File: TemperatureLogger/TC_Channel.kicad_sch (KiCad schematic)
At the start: 21 parts, among them J1 TC_BLOCK, U1 MAX31855KASA, U16 MCP1700x-330xxTT, U4 ISO7741DBQR

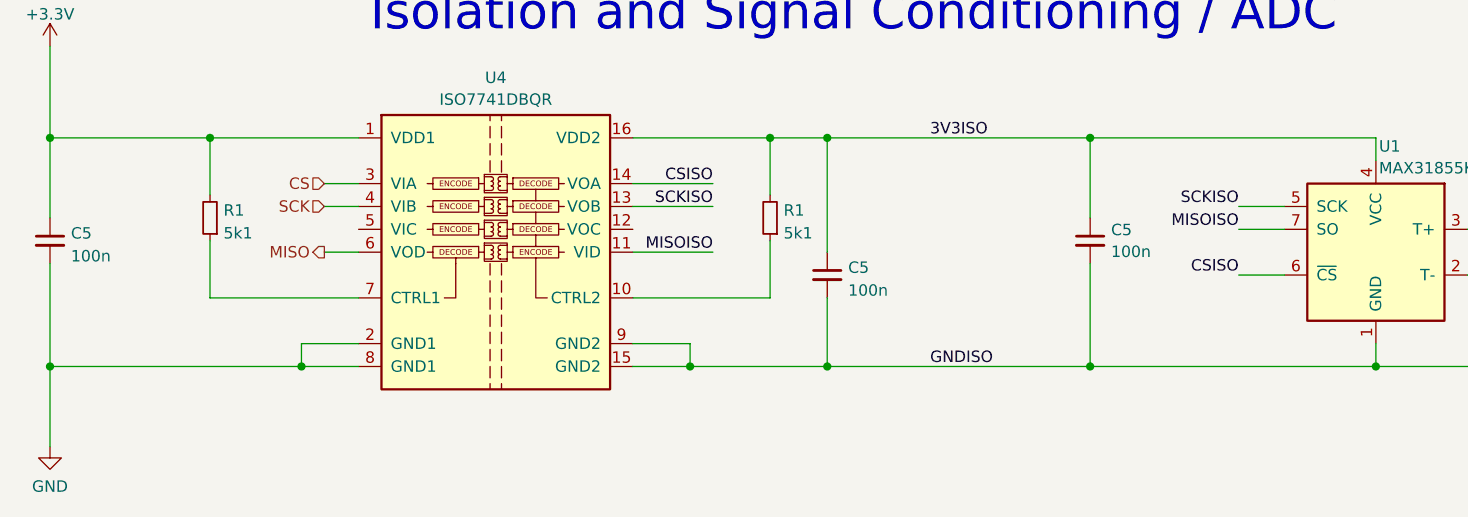
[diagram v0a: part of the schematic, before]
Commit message: added external flash and corrected issue with output disable for digital isolators
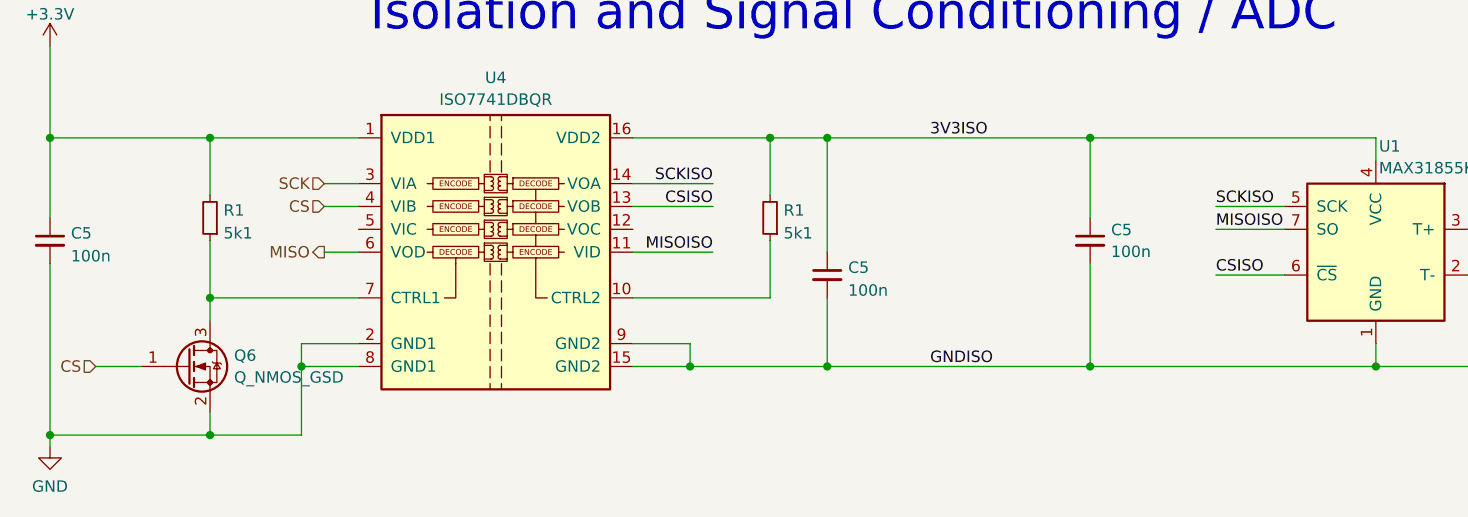
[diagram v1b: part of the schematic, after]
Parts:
- added Q6: Q_NMOS_GSD, Package_TO_SOT_SMD:SOT-23, symbol Device:Q_NMOS_GSD
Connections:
- net CS: now also U4.4 (VIB), Q6.1 (G); no longer U4.3 (VIA)
- net CSISO: now also U4.13 (VOB); no longer U4.14 (VOA)
- net GND: now also Q6.2 (S)
- net SCK: now also U4.3 (VIA); no longer U4.4 (VIB)
- net SCKISO: now also U4.14 (VOA); no longer U4.13 (VOB)
- net at R1.1, U4.7 (CTRL1): now also Q6.3 (D)
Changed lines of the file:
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@@
   (junction (at 99.06 45.72) (diameter 0) (color 0 0 0 0)
   )
+  (junction (at 53.34 147.32) (diameter 0) (color 0 0 0 0)
+  )
   (junction (at 151.13 114.3) (diameter 0) (color 0 0 0 0)
   )
@@
   (junction (at 99.06 50.8) (diameter 0) (color 0 0 0 0)
   )
+  (junction (at 35.56 147.32) (diameter 0) (color 0 0 0 0)
+  )
   (junction (at 151.13 139.7) (diameter 0) (color 0 0 0 0)
   )
@@
   (junction (at 106.68 139.7) (diameter 0) (color 0 0 0 0)
   )
-  (junction (at 35.56 139.7) (diameter 0) (color 0 0 0 0)
-  )
   (junction (at 121.92 114.3) (diameter 0) (color 0 0 0 0)
   )
+  (junction (at 53.34 132.08) (diameter 0) (color 0 0 0 0)
+  )
   (junction (at 35.56 114.3) (diameter 0) (color 0 0 0 0)
   )
@@
     (stroke (width 0) (type default))
   )
+  (wire (pts (xy 63.5 147.32) (xy 63.5 139.7))
+    (stroke (width 0) (type default))
+  )
   (wire (pts (xy 109.22 69.85) (xy 119.38 69.85))
     (stroke (width 0) (type default))
@@
     (stroke (width 0) (type default))
   )
+  (wire (pts (xy 53.34 147.32) (xy 63.5 147.32))
+    (stroke (width 0) (type default))
+  )
+  (wire (pts (xy 53.34 132.08) (xy 53.34 134.62))
+    (stroke (width 0) (type default))
+  )
   (wire (pts (xy 100.33 137.16) (xy 106.68 137.16))
     (stroke (width 0) (type default))
@@
     (stroke (width 0) (type default))
   )
-  (wire (pts (xy 35.56 128.27) (xy 35.56 139.7))
-    (stroke (width 0) (type default))
-  )
   (wire (pts (xy 224.79 128.27) (xy 224.79 130.81))
     (stroke (width 0) (type default))
@@
     (stroke (width 0) (type default))
   )
-  (wire (pts (xy 35.56 139.7) (xy 63.5 139.7))
-    (stroke (width 0) (type default))
-  )
-  (wire (pts (xy 35.56 139.7) (xy 35.56 148.59))
+  (wire (pts (xy 35.56 147.32) (xy 53.34 147.32))
     (stroke (width 0) (type default))
   )
@@
     (stroke (width 0) (type default))
   )
-  (wire (pts (xy 167.64 124.46) (xy 172.72 124.46))
+  (wire (pts (xy 165.1 124.46) (xy 172.72 124.46))
     (stroke (width 0) (type default))
   )
@@
     (stroke (width 0) (type default))
   )
+  (wire (pts (xy 35.56 128.27) (xy 35.56 147.32))
+    (stroke (width 0) (type default))
+  )
   (wire (pts (xy 184.15 60.96) (xy 184.15 69.85))
     (stroke (width 0) (type default))
@@
     (stroke (width 0) (type default))
   )
-  (wire (pts (xy 167.64 129.54) (xy 172.72 129.54))
+  (wire (pts (xy 165.1 129.54) (xy 172.72 129.54))
     (stroke (width 0) (type default))
   )
@@
     (stroke (width 0) (type default))
   )
-  (wire (pts (xy 167.64 121.92) (xy 172.72 121.92))
+  (wire (pts (xy 165.1 121.92) (xy 172.72 121.92))
     (stroke (width 0) (type default))
   )
@@
     (stroke (width 0) (type default))
   )
+  (wire (pts (xy 35.56 147.32) (xy 35.56 148.59))
+    (stroke (width 0) (type default))
+  )
   (wire (pts (xy 233.68 125.73) (xy 224.79 125.73))
     (stroke (width 0) (type default))
@@
     (stroke (width 0) (type default))
   )
+  (wire (pts (xy 40.64 139.7) (xy 45.72 139.7))
+    (stroke (width 0) (type default))
+  )
   (wire (pts (xy 115.57 132.08) (xy 100.33 132.08))
     (stroke (width 0) (type default))
@@
   )
   (wire (pts (xy 35.56 114.3) (xy 53.34 114.3))
+    (stroke (width 0) (type default))
+  )
+  (wire (pts (xy 53.34 144.78) (xy 53.34 147.32))
     (stroke (width 0) (type default))
   )
@@
     (effects (font (size 1.27 1.27)) (justify right bottom))
   )
-  (label "MISOISO" (at 167.64 124.46 180) (fields_autoplaced)
-    (effects (font (size 1.27 1.27)) (justify right bottom))
-  )
-  (label "SCKISO" (at 109.22 121.92 180) (fields_autoplaced)
+  (label "MISOISO" (at 165.1 124.46 0) (fields_autoplaced)
+    (effects (font (size 1.27 1.27)) (justify left bottom))
+  )
+  (label "SCKISO" (at 109.22 119.38 180) (fields_autoplaced)
     (effects (font (size 1.27 1.27)) (justify right bottom))
   )
@@
     (effects (font (size 1.27 1.27)) (justify left bottom))
   )
-  (label "CSISO" (at 167.64 129.54 180) (fields_autoplaced)
-    (effects (font (size 1.27 1.27)) (justify right bottom))
+  (label "CSISO" (at 165.1 129.54 0) (fields_autoplaced)
+    (effects (font (size 1.27 1.27)) (justify left bottom))
   )
   (label "TC+" (at 223.52 123.19 180) (fields_autoplaced)
@@
     (effects (font (size 1.27 1.27)) (justify right bottom))
   )
-  (label "CSISO" (at 109.22 119.38 180) (fields_autoplaced)
+  (label "CSISO" (at 109.22 121.92 180) (fields_autoplaced)
     (effects (font (size 1.27 1.27)) (justify right bottom))
   )
@@
     (effects (font (size 1.27 1.27)) (justify right bottom))
   )
-  (label "SCKISO" (at 167.64 121.92 180) (fields_autoplaced)
-    (effects (font (size 1.27 1.27)) (justify right bottom))
+  (label "SCKISO" (at 165.1 121.92 0) (fields_autoplaced)
+    (effects (font (size 1.27 1.27)) (justify left bottom))
   )
   (label "GNDISO" (at 170.18 69.85 180) (fields_autoplaced)
@@
     (effects (font (size 1.27 1.27)) (justify right bottom))
   )
-  (hierarchical_label "SCK" (shape input) (at 66.04 121.92 180) (fields_autoplaced)
+  (hierarchical_label "SCK" (shape input) (at 66.04 119.38 180) (fields_autoplaced)
     (effects (font (size 1.27 1.27)) (justify right))
   )
-  (hierarchical_label "CS" (shape input) (at 66.04 119.38 180) (fields_autoplaced)
+  (hierarchical_label "CS" (shape input) (at 66.04 121.92 180) (fields_autoplaced)
     (effects (font (size 1.27 1.27)) (justify right))
   )
@@
     (effects (font (size 1.27 1.27)) (justify right))
   )
+  (hierarchical_label "CS" (shape input) (at 40.64 139.7 180) (fields_autoplaced)
+    (effects (font (size 1.27 1.27)) (justify right))
+  )
   (symbol (lib_id "Device:C_Small") (at 151.13 125.73 0) (unit 1)
     (in_bom yes) (on_board yes) (dnp no) (fields_autoplaced)
@@
         )
       )
+    )
+  )
+  (symbol (lib_id "Device:Q_NMOS_GSD") (at 50.8 139.7 0) (unit 1)
+    (in_bom yes) (on_board yes) (dnp no) (fields_autoplaced)
+    (property "Reference" "Q6" (at 56.007 138.4879 0)
+      (effects (font (size 1.27 1.27)) (justify left))
+    )
+    (property "Value" "Q_NMOS_GSD" (at 56.007 140.9121 0)
+      (effects (font (size 1.27 1.27)) (justify left))
+    )
+    (property "Footprint" "Package_TO_SOT_SMD:SOT-23" (at 55.88 137.16 0)
+      (effects (font (size 1.27 1.27)) hide)
+    )
+    (property "Datasheet" "~" (at 50.8 139.7 0)
+      (effects (font (size 1.27 1.27)) hide)
+    )
+    (pin "1")
+    (pin "2")
+    (pin "3")
+    (instances
+      (project "TemperatureLogger"
+        (path "/663cb7c3-3b78-4e89-be2e-a66756ae87a4/eb70f11c-f749-41fa-b54e-64231764011d"
+          (reference "Q6") (unit 1)
+        )
+        (path "/663cb7c3-3b78-4e89-be2e-a66756ae87a4/515c8b76-4972-4bab-8e60-356b5933ef58"
+          (reference "Q3") (unit 1)
+        )
+        (path "/663cb7c3-3b78-4e89-be2e-a66756ae87a4/6e706344-d0f2-4a2c-8dd1-73cab47aab0a"
+          (reference "Q4") (unit 1)
+        )
+        (path "/663cb7c3-3b78-4e89-be2e-a66756ae87a4/b78e416d-4726-4256-b9ae-aaf43726529a"
+          (reference "Q5") (unit 1)
+        )
+      )
